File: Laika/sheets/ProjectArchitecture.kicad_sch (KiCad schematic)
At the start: 0 parts

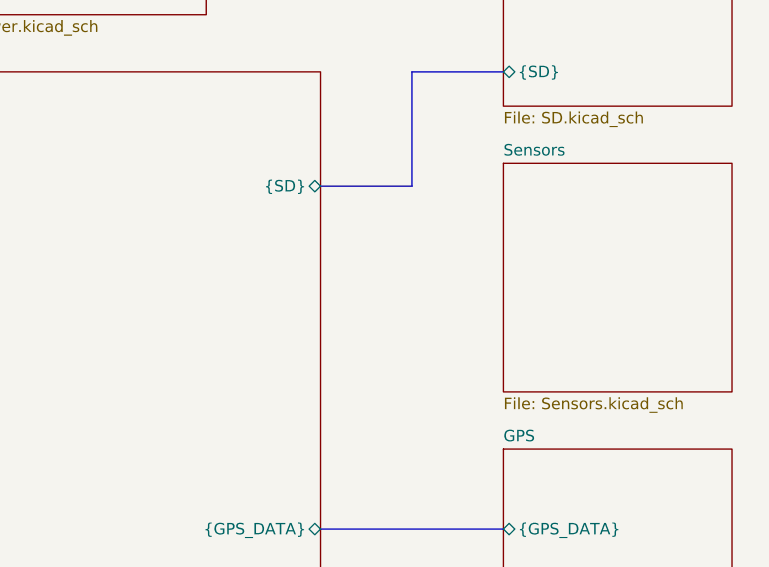
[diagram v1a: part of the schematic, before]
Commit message: Connected sensors to SPI3
Connected Sensor Bus to SPI3. Rearranged GPS reset, pps, and buzzer pins
to other 3.3V logic pins. Connected SPI chip selects. Deleted interrupt
bus from sensors due to lack of 3.3V pins.
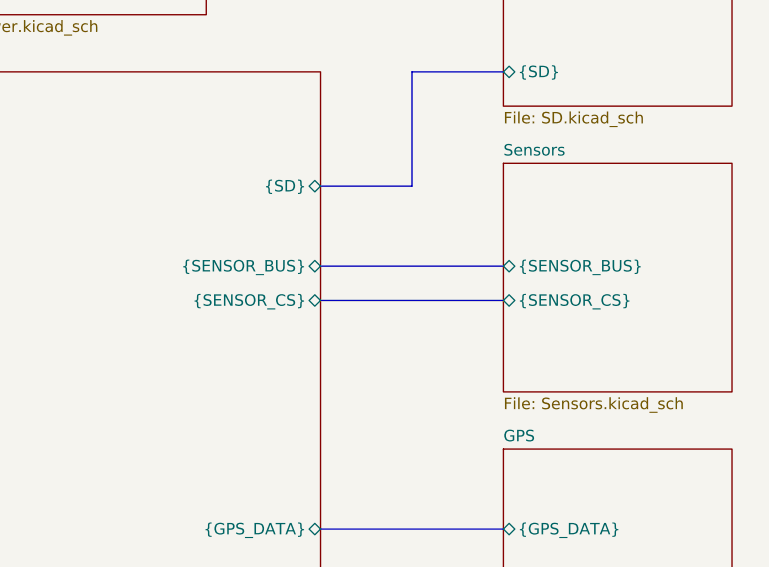
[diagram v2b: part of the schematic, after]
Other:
- sheet Sensors ports: added {SENSOR_BUS}, {SENSOR_CS}; removed none
- sheet SoC ports: added {SENSOR_BUS}, {SENSOR_CS}; removed none
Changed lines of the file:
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@@
+	(bus
+		(pts
+			(xy 139.7 72.39) (xy 160.02 72.39)
+		)
+		(stroke
+			(width 0)
+			(type default)
+		)
+	)
+	(bus
+		(pts
+			(xy 139.7 76.2) (xy 160.02 76.2)
+		)
+		(stroke
+			(width 0)
+			(type default)
+		)
+	)
 	(bus
 		(pts
@@
 			)
 		)
+		(pin "{SENSOR_BUS}" bidirectional
+			(at 139.7 72.39 0)
+			(effects
+				(font
+					(size 1.27 1.27)
+				)
+				(justify right)
+			)
+		)
+		(pin "{SENSOR_CS}" bidirectional
+			(at 139.7 76.2 0)
+			(effects
+				(font
+					(size 1.27 1.27)
+				)
+				(justify right)
+			)
+		)
 		(instances
 			(project "Laika"
@@
 			)
 		)
+		(pin "{SENSOR_BUS}" bidirectional
+			(at 160.02 72.39 180)
+			(effects
+				(font
+					(size 1.27 1.27)
+				)
+				(justify left)
+			)
+		)
+		(pin "{SENSOR_CS}" bidirectional
+			(at 160.02 76.2 180)
+			(effects
+				(font
+					(size 1.27 1.27)
+				)
+				(justify left)
+			)
+		)

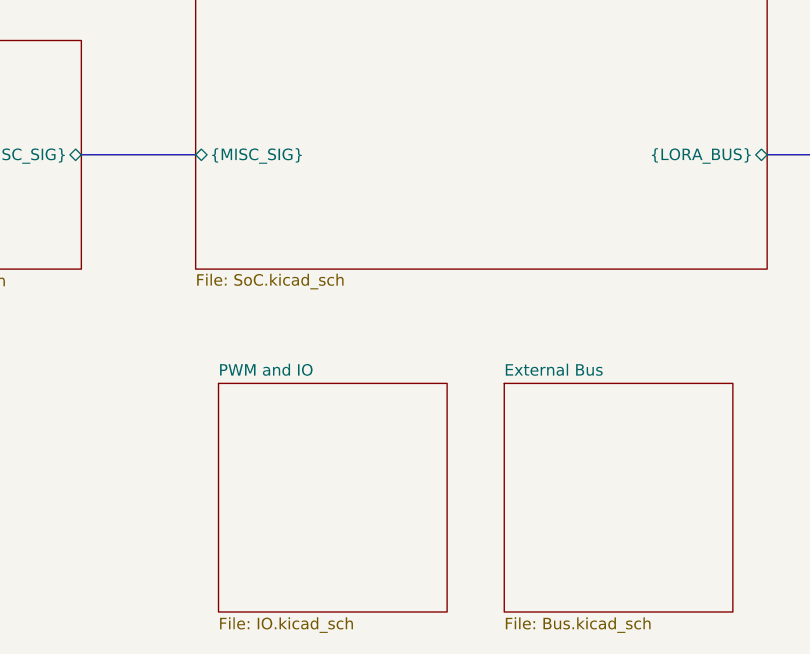
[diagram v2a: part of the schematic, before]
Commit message: Added external GPIO's for user use
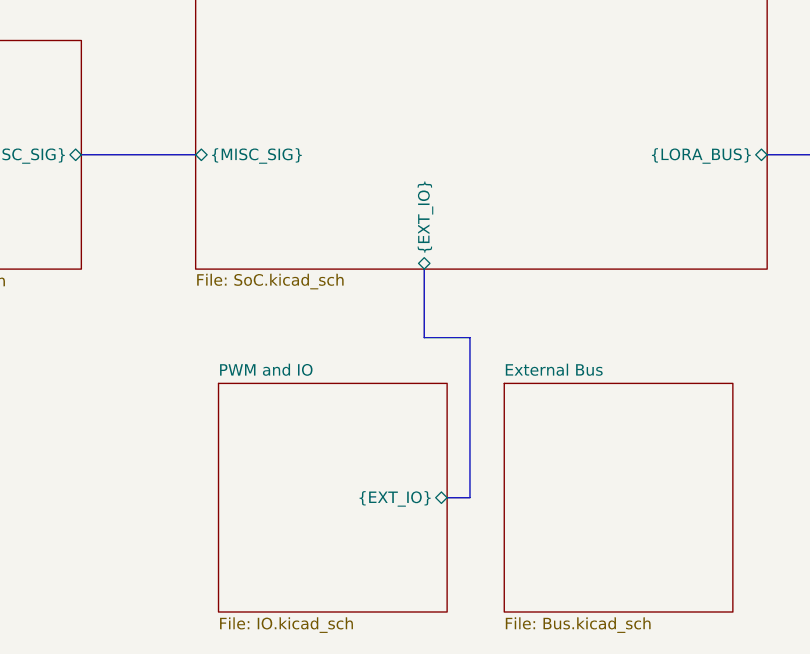
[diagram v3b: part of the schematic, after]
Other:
- sheet PWM and IO ports: added {EXT_IO}; removed none
- sheet SoC ports: added {EXT_IO}; removed none
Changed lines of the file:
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@@
+	(bus
+		(pts
+			(xy 106.68 165.1) (xy 106.68 147.32)
+		)
+		(stroke
+			(width 0)
+			(type default)
+		)
+	)
 	(bus
 		(pts
@@
 		)
 	)
+	(bus
+		(pts
+			(xy 104.14 165.1) (xy 106.68 165.1)
+		)
+		(stroke
+			(width 0)
+			(type default)
+		)
+	)
 	(wire
 		(pts
@@
 	(bus
 		(pts
+			(xy 101.6 147.32) (xy 101.6 139.7)
+		)
+		(stroke
+			(width 0)
+			(type default)
+		)
+	)
+	(bus
+		(pts
 			(xy 69.85 38.1) (xy 63.5 38.1)
 		)
@@
 		(pts
 			(xy 149.86 63.5) (xy 149.86 50.8)
+		)
+		(stroke
+			(width 0)
+			(type default)
+		)
+	)
+	(bus
+		(pts
+			(xy 106.68 147.32) (xy 101.6 147.32)
 		)
 		(stroke
@@
 			)
 		)
+		(pin "{EXT_IO}" bidirectional
+			(at 104.14 165.1 0)
+			(effects
+				(font
+					(size 1.27 1.27)
+				)
+				(justify right)
+			)
+		)
 		(instances
 			(project "Laika"
@@
 			)
 		)
+		(pin "{EXT_IO}" bidirectional
+			(at 101.6 139.7 270)
+			(effects
+				(font
+					(size 1.27 1.27)
+				)
+				(justify left)
+			)
+		)

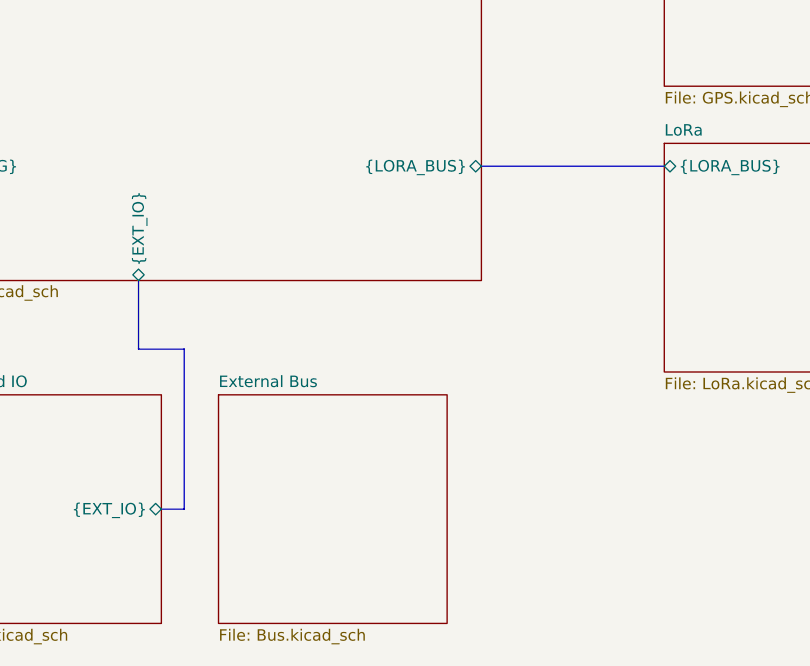
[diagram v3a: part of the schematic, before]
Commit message: Added breakout for I2C as external bus
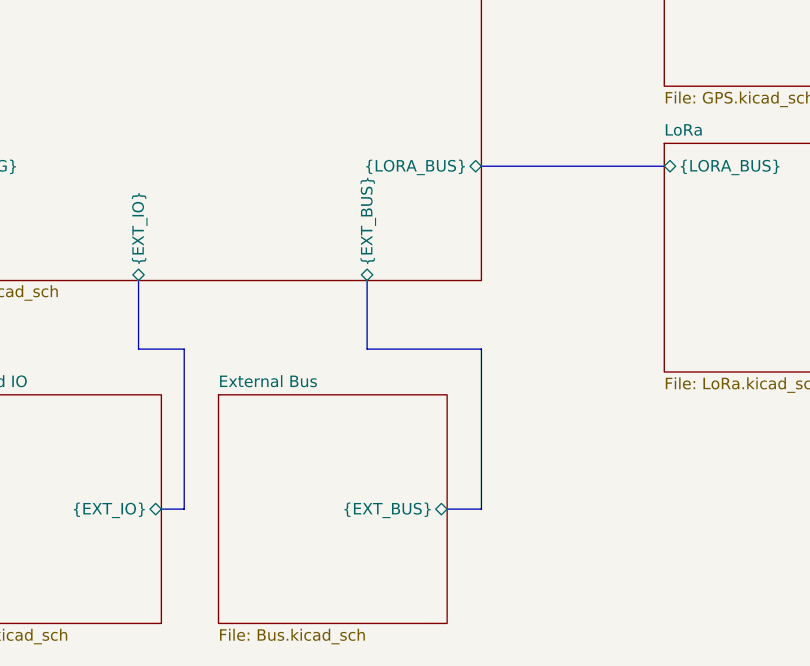
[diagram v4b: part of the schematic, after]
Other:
- sheet External Bus ports: added {EXT_BUS}; removed none
- sheet SoC ports: added {EXT_BUS}; removed none
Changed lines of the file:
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@@
+		)
+	)
+	(bus
+		(pts
+			(xy 139.7 147.32) (xy 127 147.32)
+		)
+		(stroke
+			(width 0)
+			(type default)
 		)
 	)
@@
 	(bus
 		(pts
+			(xy 139.7 165.1) (xy 139.7 147.32)
+		)
+		(stroke
+			(width 0)
+			(type default)
+		)
+	)
+	(bus
+		(pts
 			(xy 139.7 63.5) (xy 149.86 63.5)
 		)
@@
 	(bus
 		(pts
+			(xy 127 139.7) (xy 127 147.32)
+		)
+		(stroke
+			(width 0)
+			(type default)
+		)
+	)
+	(bus
+		(pts
 			(xy 101.6 147.32) (xy 101.6 139.7)
 		)
@@
 		(pts
 			(xy 139.7 21.59) (xy 139.7 29.21)
+		)
+		(stroke
+			(width 0)
+			(type default)
+		)
+	)
+	(bus
+		(pts
+			(xy 135.89 165.1) (xy 139.7 165.1)
 		)
 		(stroke
@@
 			)
 		)
+		(pin "{EXT_BUS}" bidirectional
+			(at 135.89 165.1 0)
+			(effects
+				(font
+					(size 1.27 1.27)
+				)
+				(justify right)
+			)
+		)
 		(instances
 			(project "Laika"
@@
 			(effects
 				(font
+					(size 1.27 1.27)
+				)
+				(justify left)
+			)
+		)
+		(pin "{EXT_BUS}" bidirectional
+			(at 127 139.7 270)
+			(effects
+				(font
